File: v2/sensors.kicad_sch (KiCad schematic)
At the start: 29 parts

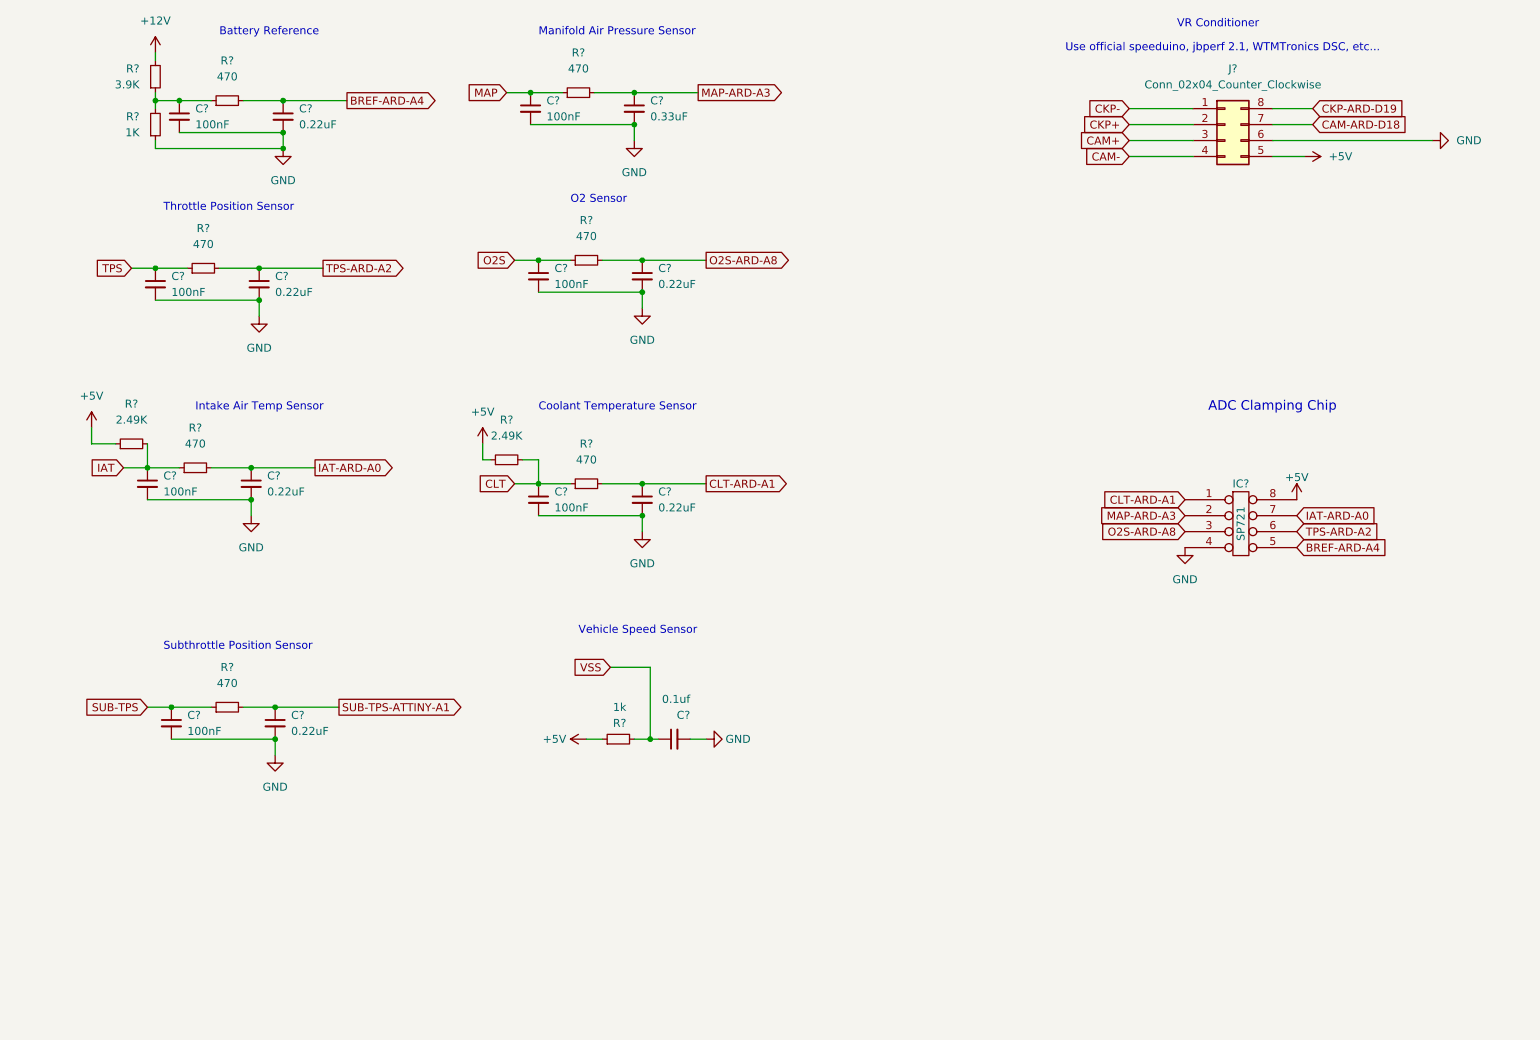
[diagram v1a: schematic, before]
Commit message: update hierarchy
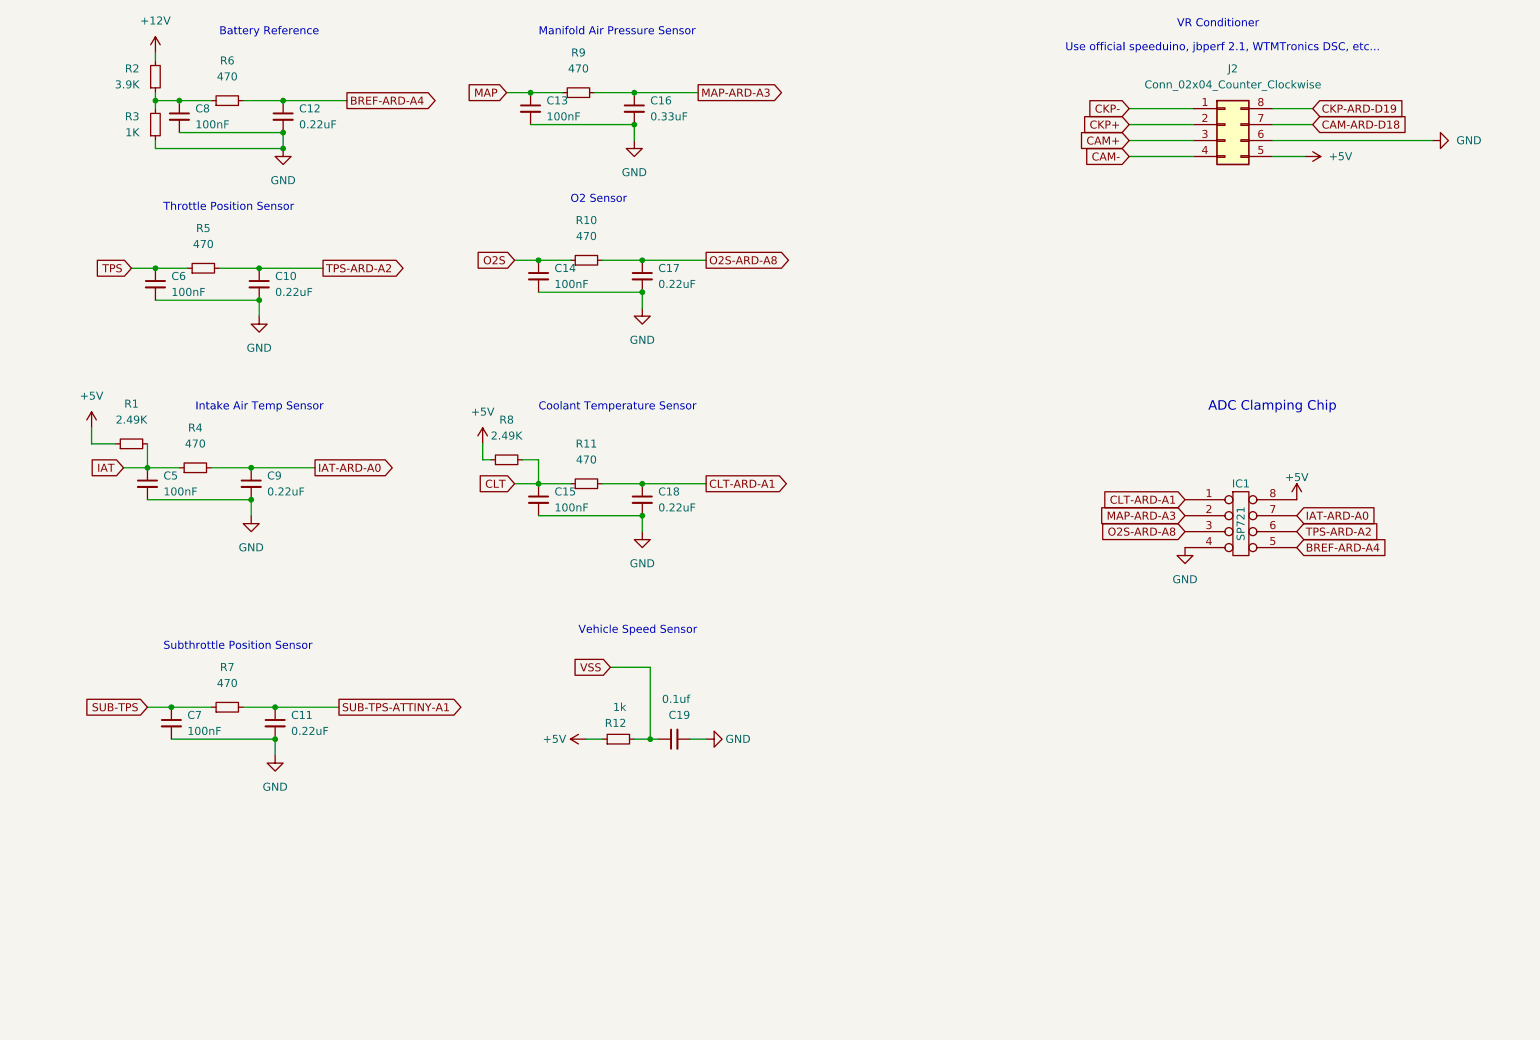
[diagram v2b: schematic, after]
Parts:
- gave numbers to parts that had none: 29

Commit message: Delete ATTiny and associated circuitry
Control the secondary throttle w/ open loop stepper idle control in the speeduino firmware
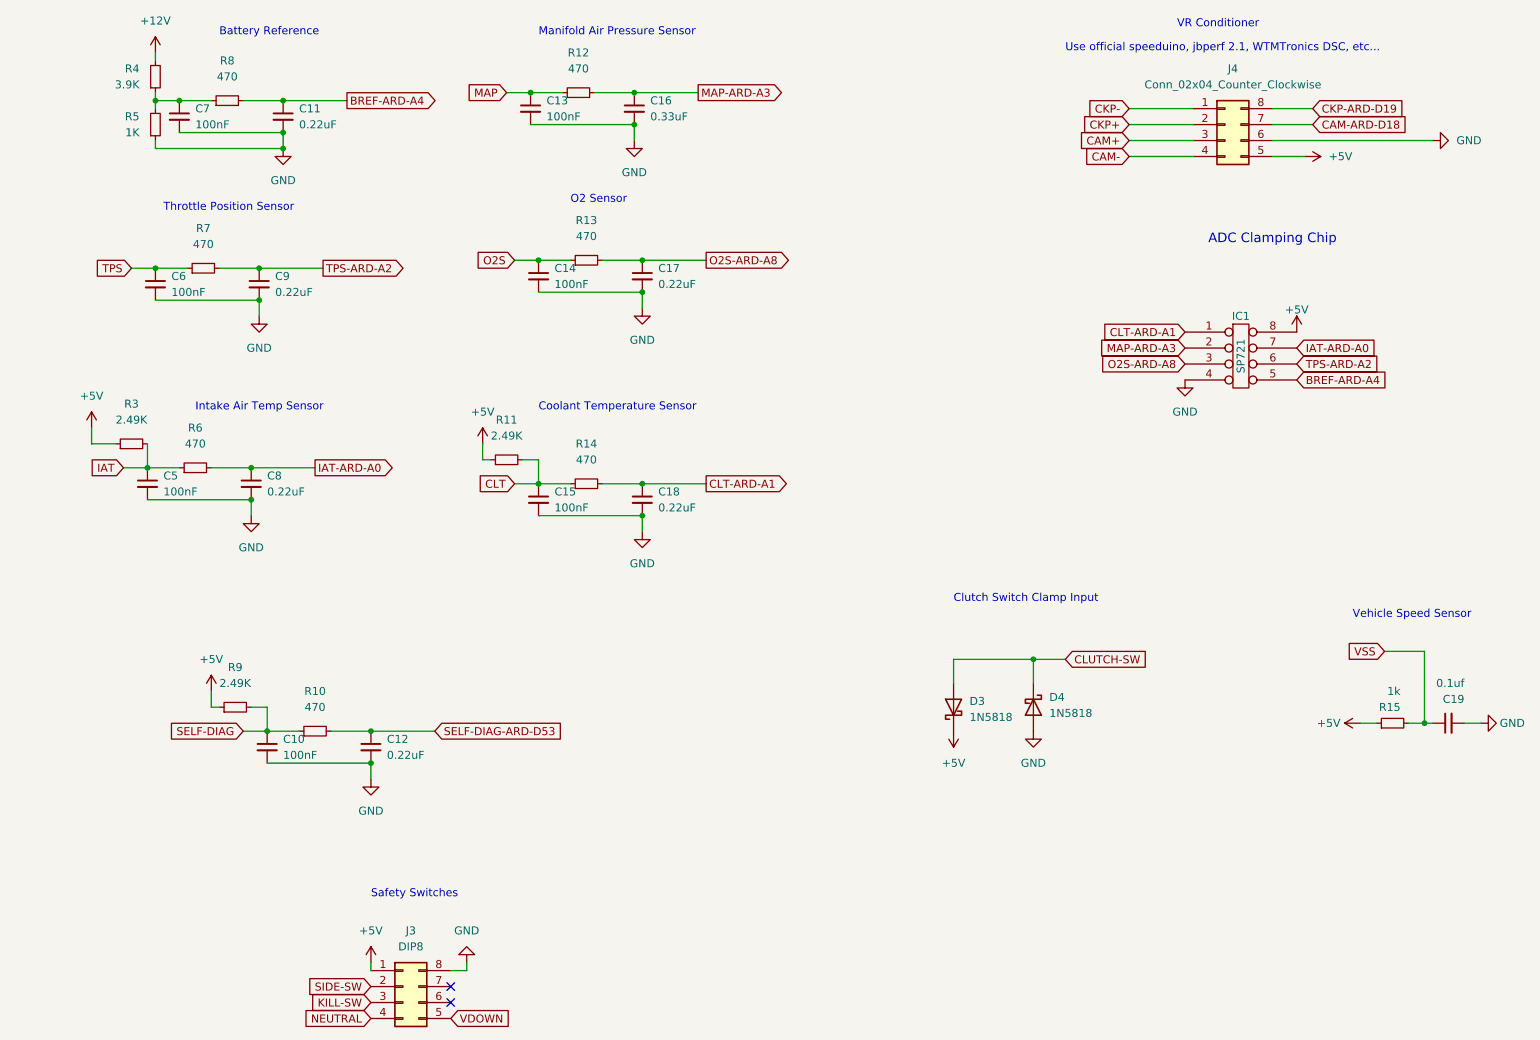
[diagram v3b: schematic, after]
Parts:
- removed C11: 0.22uF, Capacitor_SMD:C_0805_2012Metric_Pad1.18x1.45mm_HandSolder, symbol Device:C_Small
- removed C7: 100nF, Capacitor_SMD:C_0805_2012Metric_Pad1.18x1.45mm_HandSolder, symbol Device:C_Small
- removed R7: 470, Resistor_SMD:R_0805_2012Metric_Pad1.20x1.40mm_HandSolder, symbol Device:R_Small
- added C10: 100nF, Capacitor_SMD:C_0805_2012Metric_Pad1.18x1.45mm_HandSolder, symbol Device:C_Small
- added C12: 0.22uF, Capacitor_SMD:C_0805_2012Metric_Pad1.18x1.45mm_HandSolder, symbol Device:C_Small
- added D3, D4: 1N5818, Diode_THT:D_DO-41_SOD81_P7.62mm_Horizontal, symbol Device:D_Schottky
- added J3: DIP8, Package_DIP:DIP-8_W7.62mm_Socket, symbol Connector_Generic:Conn_02x04_Counter_Clockwise
- added R10: 470, Resistor_SMD:R_0805_2012Metric_Pad1.20x1.40mm_HandSolder, symbol Device:R_Small
- added R9: 2.49K, Resistor_SMD:R_0805_2012Metric_Pad1.20x1.40mm_HandSolder, symbol Device:R_Small
- renumbered C12 to C11, C8 to C7, C9 to C8, C10 to C9, J2 to J4, R8 to R11, R9 to R12, R10 to R13, R11 to R14, R12 to R15, R1 to R3, R2 to R4, R3 to R5, R4 to R6, R5 to R7, R6 to R8
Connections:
- net +5V: now also D3.1 (K), J3.1 (Pin_1), R9.1
- net GND: now also C10.2, C12.2, D4.2 (A), J3.8 (Pin_8)
- new net CLUTCH-SW: D3.2 (A), D4.1 (K)
- new net KILL-SW: J3.3 (Pin_3)
- new net NEUTRAL: J3.4 (Pin_4)
- new net SELF-DIAG: C10.1, R10.1, R9.2
- new net SELF-DIAG-ARD-D53: C12.1, R10.2
- new net SIDE-SW: J3.2 (Pin_2)
- new net VDOWN: J3.5 (Pin_5)
- no-connect marks 0 -> 2
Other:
- note added: "Clutch Switch Clamp Input"
- note added: "Safety Switches"
- note removed: "Subthrottle Position Sensor"
- moved on the sheet: C19, IC1, R15

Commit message: V2.1 is done?
Uses the JST WPZ connector footprint instead of standard
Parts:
- removed C14: 100nF, Capacitor_SMD:C_0805_2012Metric_Pad1.18x1.45mm_HandSolder, symbol Device:C_Small
- removed C17: 0.22uF, Capacitor_SMD:C_0805_2012Metric_Pad1.18x1.45mm_HandSolder, symbol Device:C_Small
- removed R13: 470, Resistor_SMD:R_0805_2012Metric_Pad1.20x1.40mm_HandSolder, symbol Device:R_Small
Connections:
- net BREF-ARD-A4: now also C11.2; no longer C11.1
- net GND: now also C11.1; no longer C11.2
- net KILL-SW: now also J3.2 (Pin_2); no longer J3.3 (Pin_3)
- net NEUTRAL: now also J3.5 (Pin_5); no longer J3.4 (Pin_4)
- net SIDE-SW: now also J3.3 (Pin_3); no longer J3.2 (Pin_2)
- net VDOWN: now also J3.4 (Pin_4); no longer J3.5 (Pin_5)
- net ARDUINO-RST: now reaches J3.7 (Pin_7)
- net O2S-ARD-A8: no longer names the net of IC1.3 (P3)
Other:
- note removed: "O2 Sensor"
- moved on the sheet: C11

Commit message: Re-add traces for oxygen sensor
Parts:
- added C?: 0.33uF, Capacitor_SMD:C_0805_2012Metric_Pad1.18x1.45mm_HandSolder, symbol Device:C_Small
- added C?: 100nF, Capacitor_SMD:C_0805_2012Metric_Pad1.18x1.45mm_HandSolder, symbol Device:C_Small
- added R?: 470, Resistor_SMD:R_0805_2012Metric_Pad1.20x1.40mm_HandSolder, symbol Device:R_Small
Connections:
- net GND: now also C?.2, C?.2
- net O2S-ARD-A8: now reaches IC1.3 (P3)
- net O2S-ARD-A8: now also C?.1, R?.2
- new net O2S: C?.1, R?.1
- no-connect marks 2 -> 1
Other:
- moved on the sheet: C10, C12, R10, R9

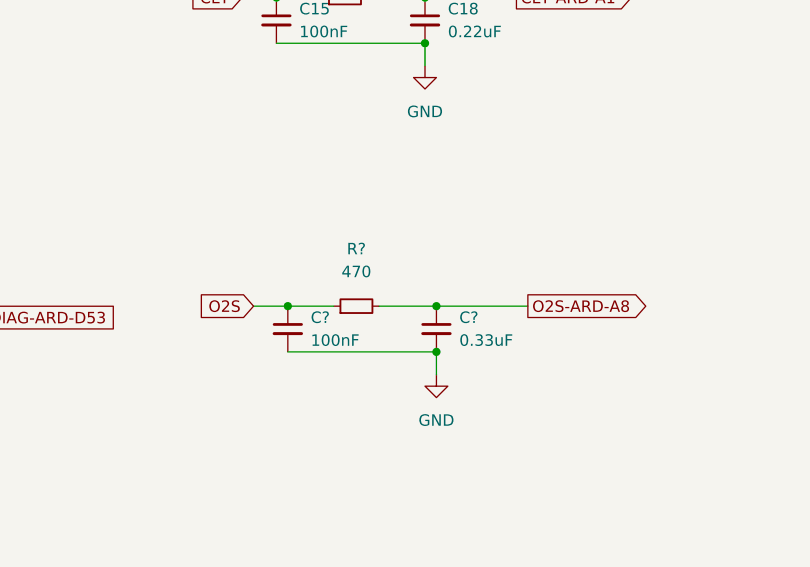
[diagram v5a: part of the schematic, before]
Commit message: Add control of air switching valve
Plus a jumper to lock the valve closed
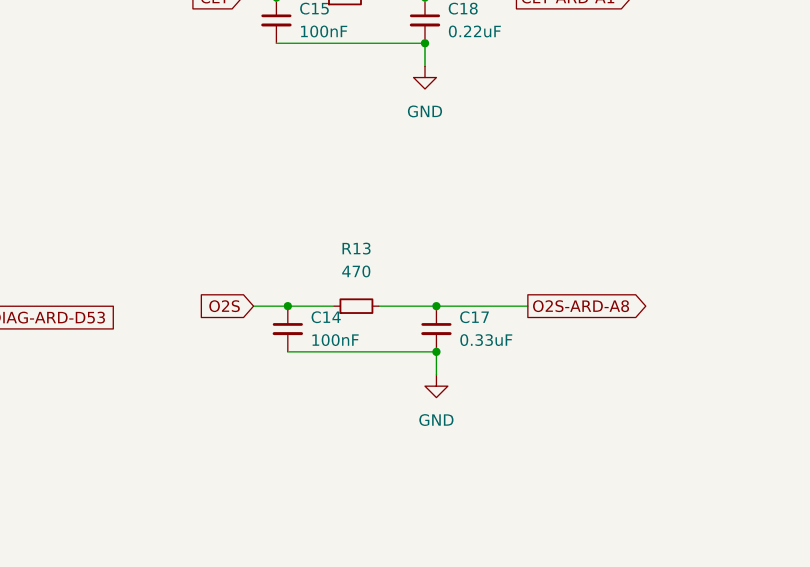
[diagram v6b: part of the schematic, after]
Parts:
- gave numbers to parts that had none: 3
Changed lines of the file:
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@@
   (symbol (lib_id "Device:R_Small") (at 109.22 129.54 90) (unit 1)
     (in_bom yes) (on_board yes) (fields_autoplaced)
-    (property "Reference" "R?" (id 0) (at 109.22 123.19 90))
+    (property "Reference" "R13" (id 0) (at 109.22 123.19 90))
     (property "Value" "470" (id 1) (at 109.22 125.73 90))
     (property "Footprint" "Resistor_SMD:R_0805_2012Metric_Pad1.20x1.40mm_HandSolder" (id 2) (at 109.22 129.54 0)
@@
   (symbol (lib_id "Device:C_Small") (at 118.11 132.08 0) (unit 1)
     (in_bom yes) (on_board yes) (fields_autoplaced)
-    (property "Reference" "C?" (id 0) (at 120.65 130.8162 0)
+    (property "Reference" "C17" (id 0) (at 120.65 130.8162 0)
       (effects (font (size 1.27 1.27)) (justify left))
     )
@@
   (symbol (lib_id "power:GND") (at 118.11 137.16 0) (unit 1)
     (in_bom yes) (on_board yes) (fields_autoplaced)
-    (property "Reference" "#PWR?" (id 0) (at 118.11 143.51 0)
+    (property "Reference" "#PWR024" (id 0) (at 118.11 143.51 0)
       (effects (font (size 1.27 1.27)) hide)
     )
@@
   (symbol (lib_id "Device:C_Small") (at 101.6 132.08 0) (unit 1)
     (in_bom yes) (on_board yes) (fields_autoplaced)
-    (property "Reference" "C?" (id 0) (at 104.14 130.8162 0)
-      (effects (font (size 1.27 1.27)) (justify left))
-    )
+    (property "Reference" "C14" (id 0) (at 104.14 130.8162 0)
+      (effects (font (size 1.27 1.27)) (justify left))
+    )

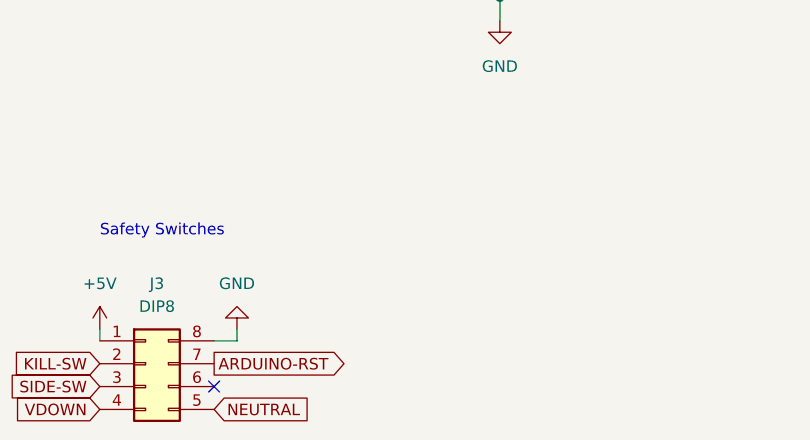
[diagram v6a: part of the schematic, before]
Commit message: Add reset protection jumper
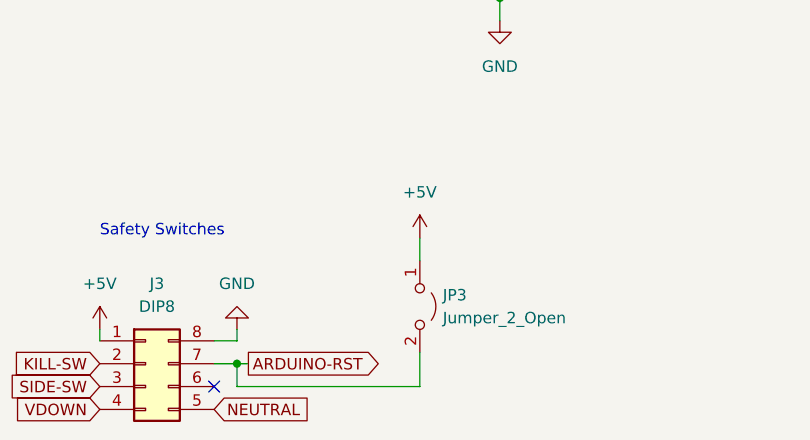
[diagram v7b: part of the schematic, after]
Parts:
- added JP3: Jumper_2_Open, Jumper:SolderJumper-2_P1.3mm_Open_Pad1.0x1.5mm, symbol Jumper:Jumper_2_Open
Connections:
- net +5V: now also JP3.1 (A)
- net ARDUINO-RST: now also JP3.2 (B)
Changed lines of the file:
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@@
   (junction (at 116.84 100.33) (diameter 0) (color 0 0 0 0)
+  )
+  (junction (at 88.9 175.26) (diameter 0) (color 0 0 0 0)
   )
   (junction (at 115.57 33.02) (diameter 0) (color 0 0 0 0)
@@
     (stroke (width 0) (type default) (color 0 0 0 0))
   )
+  (wire (pts (xy 90.17 175.26) (xy 88.9 175.26))
+    (stroke (width 0) (type default) (color 0 0 0 0))
+  )
   (wire (pts (xy 39.37 66.04) (xy 55.88 66.04))
     (stroke (width 0) (type default) (color 0 0 0 0))
@@
     (stroke (width 0) (type default) (color 0 0 0 0))
   )
+  (wire (pts (xy 88.9 175.26) (xy 88.9 177.8))
+    (stroke (width 0) (type default) (color 0 0 0 0))
+  )
   (wire (pts (xy 99.06 38.1) (xy 115.57 38.1))
     (stroke (width 0) (type default) (color 0 0 0 0))
@@
     (stroke (width 0) (type default) (color 0 0 0 0))
   )
+  (wire (pts (xy 88.9 177.8) (xy 109.22 177.8))
+    (stroke (width 0) (type default) (color 0 0 0 0))
+  )
+  (wire (pts (xy 88.9 175.26) (xy 86.36 175.26))
+    (stroke (width 0) (type default) (color 0 0 0 0))
+  )
   (wire (pts (xy 217.17 38.1) (xy 223.52 38.1))
     (stroke (width 0) (type default) (color 0 0 0 0))
@@
     (stroke (width 0) (type default) (color 0 0 0 0))
   )
+  (wire (pts (xy 109.22 161.29) (xy 109.22 163.83))
+    (stroke (width 0) (type default) (color 0 0 0 0))
+  )
   (wire (pts (xy 29.21 86.36) (xy 29.21 88.9))
     (stroke (width 0) (type default) (color 0 0 0 0))
@@
   )
   (wire (pts (xy 111.76 129.54) (xy 118.11 129.54))
+    (stroke (width 0) (type default) (color 0 0 0 0))
+  )
+  (wire (pts (xy 109.22 173.99) (xy 109.22 177.8))
     (stroke (width 0) (type default) (color 0 0 0 0))
   )
@@
     )
   )
-  (global_label "ARDUINO-RST" (shape output) (at 86.36 175.26 0) (fields_autoplaced)
-    (effects (font (size 1.27 1.27)) (justify left))
-    (property "Intersheet References" "${INTERSHEET_REFS}" (id 0) (at 102.0174 175.1806 0)
+  (global_label "ARDUINO-RST" (shape output) (at 90.17 175.26 0) (fields_autoplaced)
+    (effects (font (size 1.27 1.27)) (justify left))
+    (property "Intersheet References" "${INTERSHEET_REFS}" (id 0) (at 105.8274 175.1806 0)
       (effects (font (size 1.27 1.27)) (justify left) hide)
     )
@@
     (pin "1")
   )
+  (symbol (lib_id "power:+5V") (at 109.22 161.29 0) (unit 1)
+    (in_bom yes) (on_board yes) (fields_autoplaced)
+    (property "Reference" "#PWR052" (id 0) (at 109.22 165.1 0)
+      (effects (font (size 1.27 1.27)) hide)
+    )
+    (property "Value" "+5V" (id 1) (at 109.22 156.21 0))
+    (property "Footprint" "" (id 2) (at 109.22 161.29 0)
+      (effects (font (size 1.27 1.27)) hide)
+    )
+    (property "Datasheet" "" (id 3) (at 109.22 161.29 0)
+      (effects (font (size 1.27 1.27)) hide)
+    )
+    (pin "1")
+  )
   (symbol (lib_id "Device:R_Small") (at 46.99 60.96 90) (unit 1)
     (in_bom yes) (on_board yes) (fields_autoplaced)
@@
     (pin "1")
   )
+  (symbol (lib_id "Jumper:Jumper_2_Open") (at 109.22 168.91 270) (unit 1)
+    (in_bom yes) (on_board yes) (fields_autoplaced)
+    (property "Reference" "JP3" (id 0) (at 111.76 167.6399 90)
+      (effects (font (size 1.27 1.27)) (justify left))
+    )
+    (property "Value" "Jumper_2_Open" (id 1) (at 111.76 170.1799 90)
+      (effects (font (size 1.27 1.27)) (justify left))
+    )
+    (property "Footprint" "Jumper:SolderJumper-2_P1.3mm_Open_Pad1.0x1.5mm" (id 2) (at 109.22 168.91 0)
+      (effects (font (size 1.27 1.27)) hide)
+    )
+    (property "Datasheet" "~" (id 3) (at 109.22 168.91 0)
+      (effects (font (size 1.27 1.27)) hide)
+    )
+    (pin "1")
+    (pin "2")
+  )
   (symbol (lib_id "Device:R_Small") (at 107.95 95.25 90) (unit 1)
